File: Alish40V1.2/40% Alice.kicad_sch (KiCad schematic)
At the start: 95 parts, among them J1 Conn_01x03, K1 KEYSW, K10 KEYSW, K11 KEYSW, K12 KEYSW, K13 KEYSW, K14 KEYSW, K15 KEYSW, K16 KEYSW, K17 KEYSW, K18 KEYSW, K19 KEYSW, K2 KEYSW, K20 KEYSW, K21 KEYSW, K22 KEYSW, K23 KEYSW, K24 KEYSW, K25 KEYSW, K26 KEYSW, K27 KEYSW, K28 KEYSW, K29 KEYSW, K3 KEYSW, K30 KEYSW, K31 KEYSW, K32 KEYSW, K33 KEYSW, K34 KEYSW, K35 KEYSW, K36 KEYSW, K37 KEYSW, K38 KEYSW, K39 KEYSW, K4 KEYSW, K40 KEYSW, K41 KEYSW, K42 KEYSW, K43 KEYSW, K44 KEYSW, K45 KEYSW, K46 KEYSW, K47 KEYSW, K5 KEYSW, K6 KEYSW, K7 KEYSW, K8 KEYSW, K9 KEYSW, U1 ProMicro

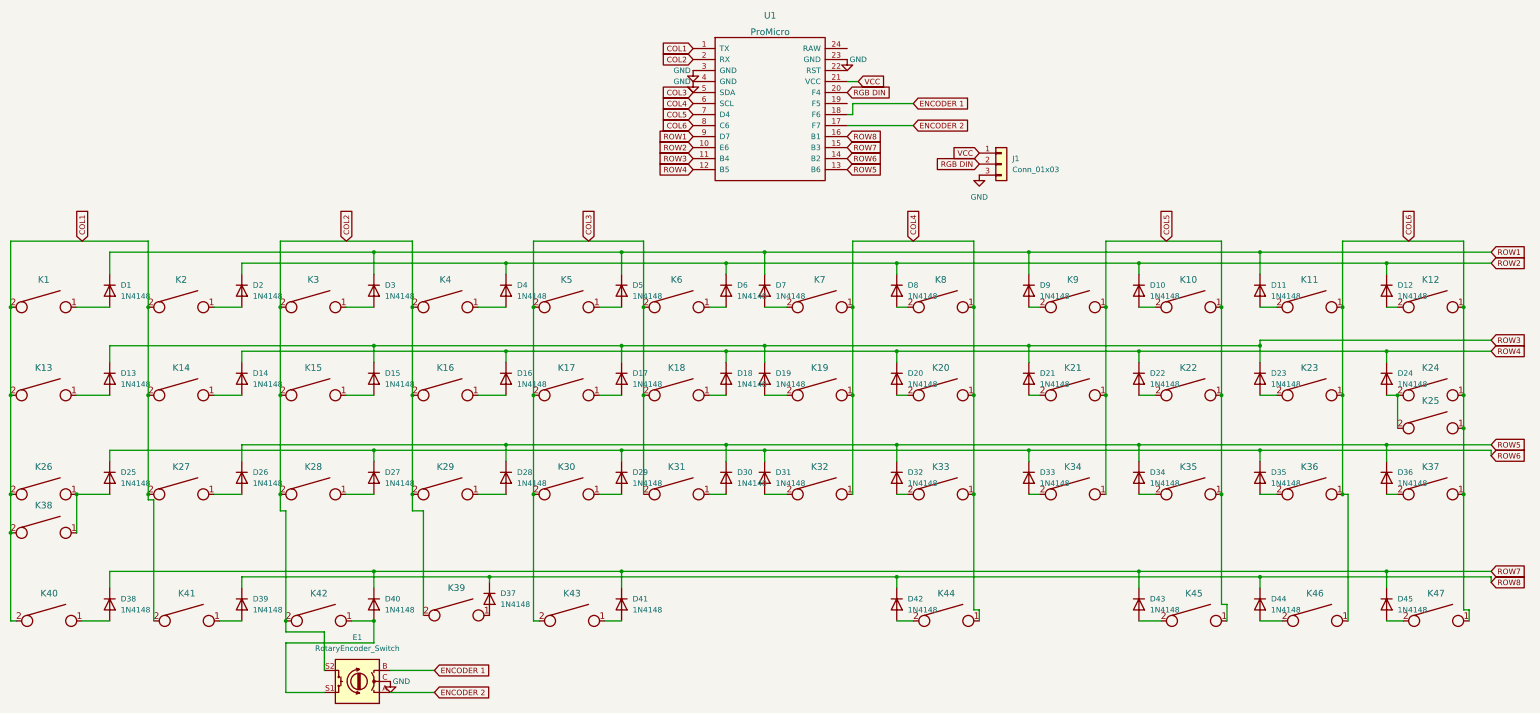
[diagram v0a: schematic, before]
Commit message: Updated PCB and Schematic
Changed Reference Designators, updated footprints, fixed several routing issues, added Reed X (silly), added my footprints, moved encoder slightly, tightened up QAZ to WSX spacing.
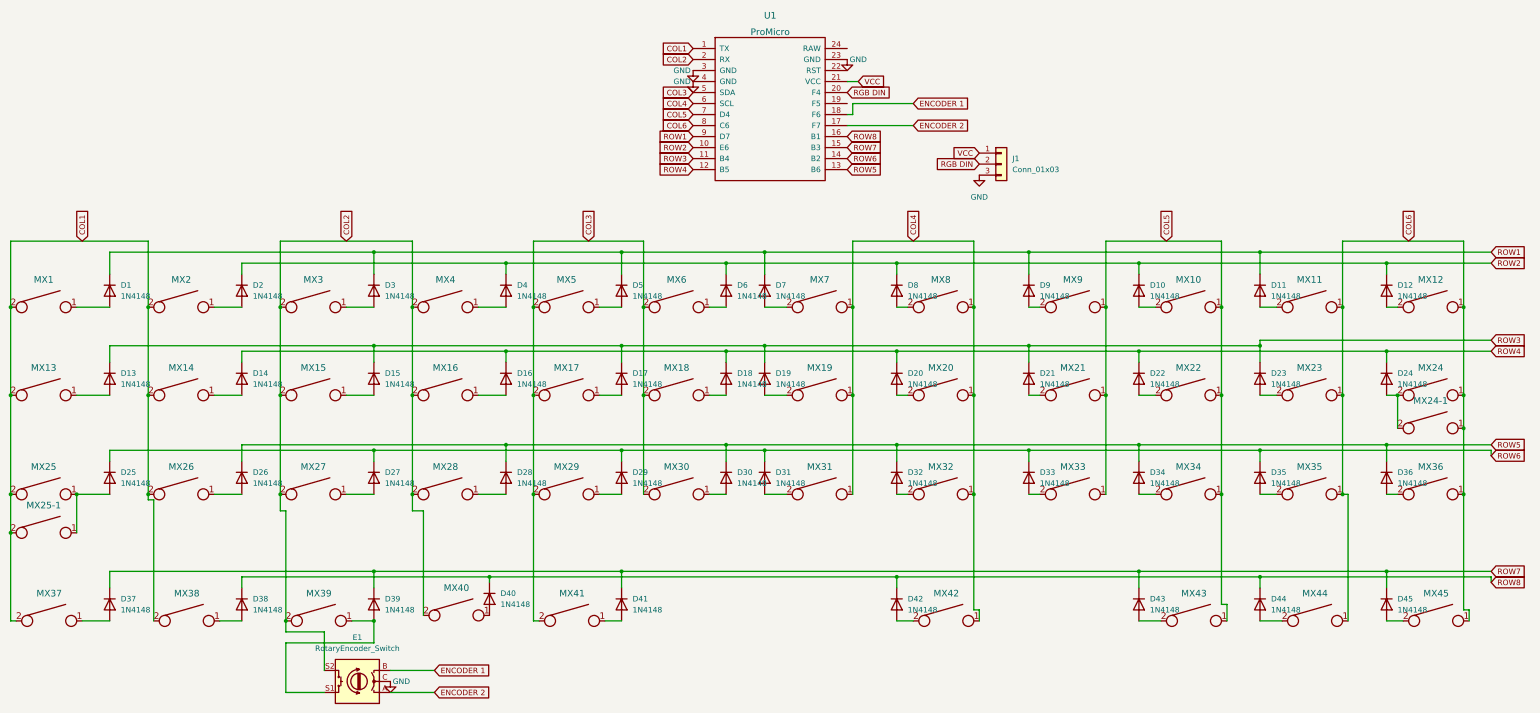
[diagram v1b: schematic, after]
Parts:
- renumbered D38 to D37, D39 to D38, D40 to D39, D37 to D40, K1 to MX1, K10 to MX10, K11 to MX11, K12 to MX12, K13 to MX13, K14 to MX14, K15 to MX15, K16 to MX16, K17 to MX17, K18 to MX18, K19 to MX19, K2 to MX2, K20 to MX20, K21 to MX21, K22 to MX22, K23 to MX23, K24 to MX24, K25 to MX24-1, K26 to MX25, K38 to MX25-1, K27 to MX26, K28 to MX27, K29 to MX28, K30 to MX29, K3 to MX3, K31 to MX30, K32 to MX31, K33 to MX32, K34 to MX33, K35 to MX34, K36 to MX35, K37 to MX36, K40 to MX37, K41 to MX38, K42 to MX39, K4 to MX4, K39 to MX40, K43 to MX41, K44 to MX42, K45 to MX43, K46 to MX44, K47 to MX45, K5 to MX5, K6 to MX6, K7 to MX7, K8 to MX8, K9 to MX9
